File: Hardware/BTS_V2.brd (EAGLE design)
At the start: 113 x 79.4 mm, 57 parts, among them IC1 TPA3140D2PWP, IC2 BLK-MD-SPK-B, J1 SPKR_OUT, J2 RN52BoB_R, J3 RN52BoB_L, J6 HC-05, J7 PRT-10474, T3_2 TEENSY_3.1-3.2_DIL

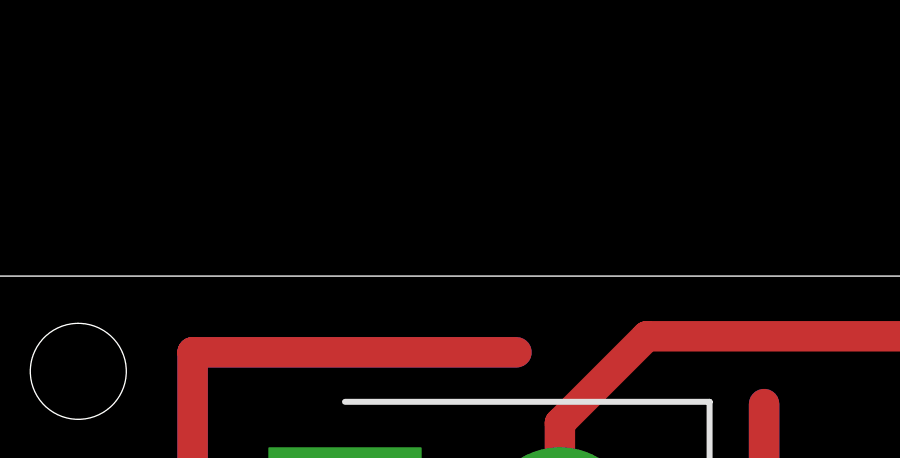
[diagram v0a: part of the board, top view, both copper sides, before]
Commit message: Created new XT-60 connector
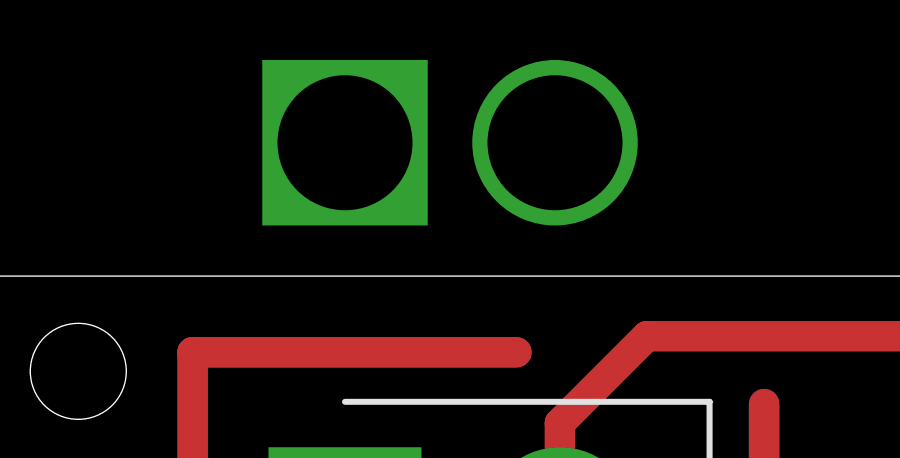
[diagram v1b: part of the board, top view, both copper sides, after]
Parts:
- added U$1: HK_XT-60, myLib:HOBBYKING_XT-60
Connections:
- net GND: now also U$1.P$1
- net VIN: now also U$1.P$2
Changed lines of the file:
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@@
 <element name="J4" library="SparkFun-Connectors" library_urn="urn:adsk.eagle:library:513" package="1X14" package3d_urn="urn:adsk.eagle:package:38183/1" value="" x="109.855" y="17.78" rot="R90"/>
 <element name="R16" library="resistor" library_urn="urn:adsk.eagle:library:348" package="R0603" package3d_urn="urn:adsk.eagle:package:26057/1" value="100R" x="100.33" y="45.72" rot="R180"/>
+<element name="U$1" library="myLib" package="HOBBYKING_XT-60" value="HK_XT-60" x="12.065" y="83.82"/>
 </elements>
 <signals>
@@
 <wire x1="33.79" y1="30.48" x2="38.735" y2="30.48" width="0.4064" layer="1"/>
 <contactref element="J4" pad="13"/>
+<contactref element="U$1" pad="P$1"/>
 <wire x1="99.695" y1="57.785" x2="109.855" y2="48.26" width="0" layer="19" extent="1-1"/>
 <wire x1="91.313" y1="52.07" x2="99.695" y2="57.785" width="0" layer="19" extent="1-1"/>
@@
 <wire x1="75.565" y1="26.924" x2="75.285" y2="26.3502125" width="0" layer="19" extent="1-1"/>
 <wire x1="71.755" y1="26.924" x2="72.035" y2="26.3502125" width="0" layer="19" extent="1-1"/>
+<wire x1="72.3646" y1="27.94" x2="71.29000625" y2="28.40499375" width="0" layer="19" extent="1-1"/>
 <wire x1="75.565" y1="28.956" x2="74.93" y2="27.94" width="0" layer="19" extent="1-1"/>
+<wire x1="70.1294" y1="27.94" x2="71.29000625" y2="28.40499375" width="0" layer="19" extent="1-1"/>
+<wire x1="76.9366" y1="27.94" x2="75.565" y2="26.924" width="0" layer="19" extent="1-1"/>
 <wire x1="75.145" y1="13.335" x2="75.285" y2="25.002" width="0" layer="19" extent="1-1"/>
 <wire x1="69.635" y1="13.335" x2="75.145" y2="13.335" width="0" layer="19" extent="1-1"/>
@@
 <wire x1="12.065" y1="71.12" x2="12.065" y2="52.705" width="0" layer="19" extent="1-1"/>
 <wire x1="12.7" y1="13.335" x2="33.64" y2="29.03" width="0" layer="19" extent="1-1"/>
+<wire x1="12.065" y1="83.82" x2="12.7" y2="13.335" width="0" layer="19" extent="1-1"/>
 </signal>
 <signal name="N$1">
@@
 <wire x1="19.228" y1="74.473" x2="22.1234" y2="77.3684" width="1.016" layer="1"/>
 <wire x1="22.1234" y1="77.3684" x2="55.245" y2="77.3684" width="1.016" layer="1"/>
+<contactref element="U$1" pad="P$2"/>
+<wire x1="19.065" y1="83.82" x2="19.228" y2="71.12" width="0" layer="19" extent="1-1"/>
 </signal>
 <signal name="PWRGOOD">

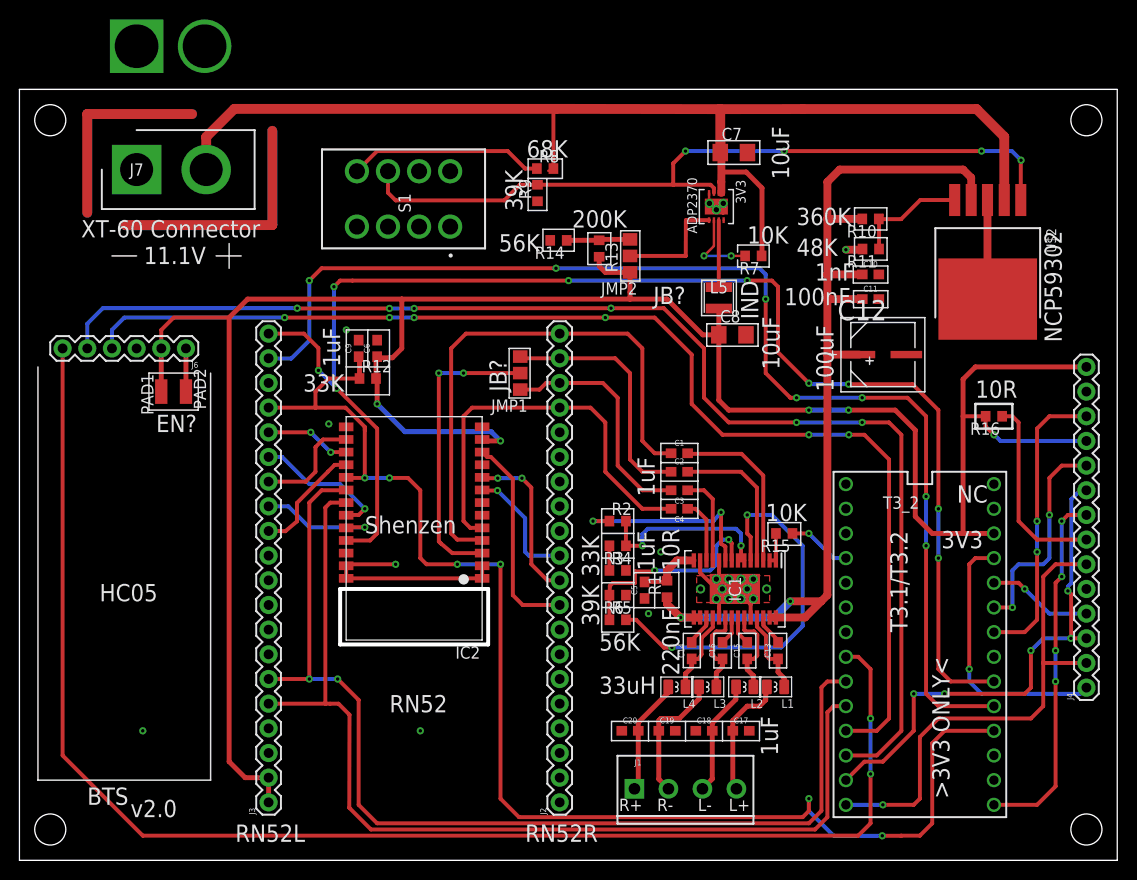
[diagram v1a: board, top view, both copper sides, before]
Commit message: added PA test code & modified V2 board files
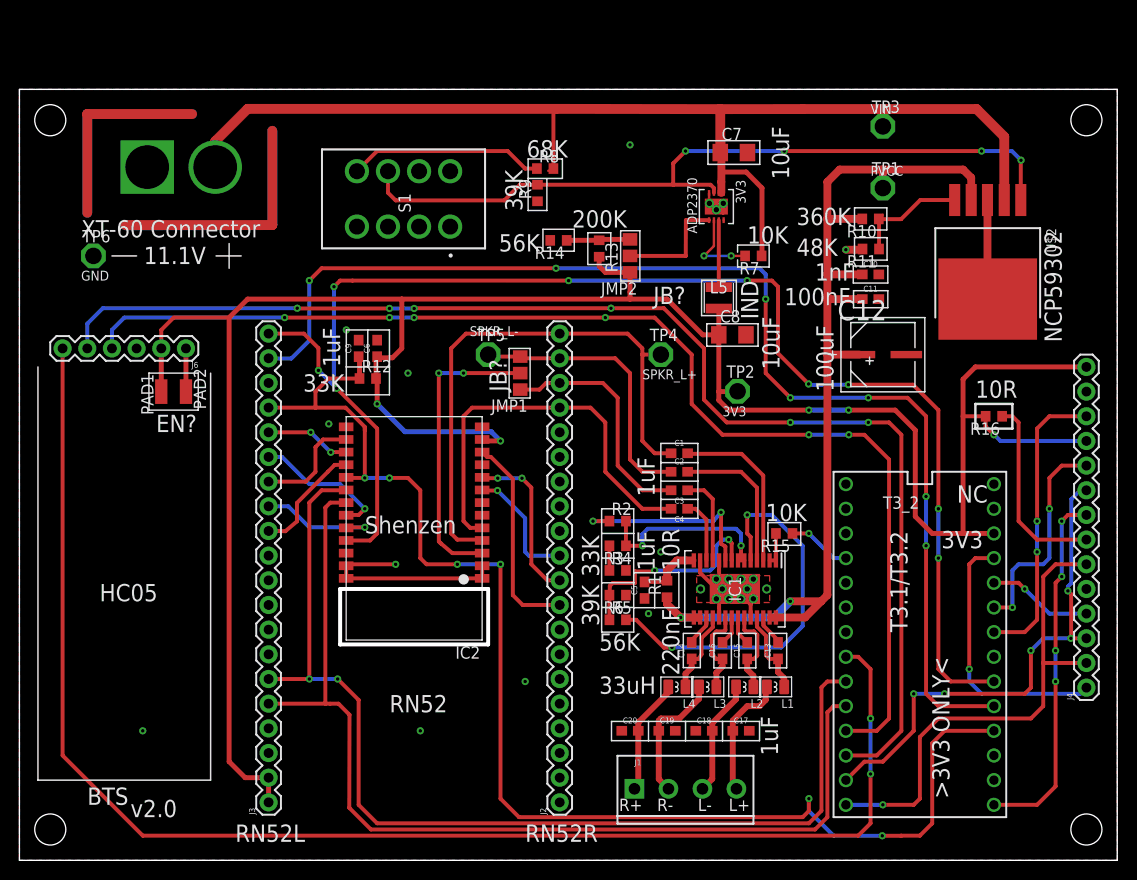
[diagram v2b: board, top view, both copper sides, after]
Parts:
- removed J7: PRT-10474, PRT-10474:SHDR2W320P716_1X2_1574X813X158
- added TP1, TP2, TP3, TP4, TP5, TP6: TPSPAD1-17, testpad:P1-17
- J4: value (none) -> TFT_CONNECTION
- moved U$1 12.5 mm to (13.2, 71.4)
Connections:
- net 3V3: now also TP2.TP
- net GND: now also TP6.TP; no longer J7.1
- net PVCC: now also TP1.TP
- net SPKR_L+: now also TP4.TP
- net SPKR_L-: now also TP5.TP
- net VIN: now also TP3.TP; no longer J7.2
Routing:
- net SPKR_L-: track 25.7 -> 29.0 mm
- net 3V3: track 248.3 -> 250.2 mm
- net PVCC: track 102.4 -> 104.3 mm
- net SPKR_L+: track 56.5 -> 58.4 mm
- net GND: vias 23 -> 26
- added copper zone on layer 16, net GND
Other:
- board text added: "GND"
- board text added: "PVCC"
- board text added: "SPKR_L+"
- board text added: "SPKR_L-"
- board text added: "VIN"

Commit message: Further error fixed
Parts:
- moved J6 12.7 mm to (4.45, 52.1), turned to 0 degrees
- moved PAD2 12.7 mm to (4.45, 48.3), turned to 0 degrees
- moved PAD1 7.62 mm to (6.99, 48.3), turned to 180 degrees
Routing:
- net HC_UART_RX: track 132.8 -> 157.4 mm
- net 3V3: track 250.2 -> 257.8 mm
- net HC_UART_TX: track 123.1 -> 121.2 mm
- net STATE: track 148.0 -> 149.3 mm
- net EN: track 4.45 -> 3.81 mm
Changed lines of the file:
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@@
 <wire x1="68.58" y1="14.3002" x2="68.58" y2="12.319" width="0.1524" layer="21"/>
 <wire x1="72.39" y1="14.3002" x2="72.39" y2="12.319" width="0.1524" layer="21"/>
-<text x="14.0716" y="44.0944" size="1.778" layer="21" font="vector">EN?</text>
+<text x="3.9116" y="43.4594" size="1.778" layer="21" font="vector">EN?</text>
 <wire x1="66.04" y1="42.926" x2="69.85" y2="42.926" width="0.1524" layer="21"/>
 <wire x1="69.85" y1="42.926" x2="69.85" y2="40.9448" width="0.1524" layer="21"/>
@@
 <wire x1="78.8162" y1="24.0284" x2="78.105" y2="24.0284" width="0.1524" layer="21"/>
 <wire x1="68.5038" y1="24.0284" x2="69.1896" y2="24.0284" width="0.1524" layer="21"/>
-<wire x1="13.335" y1="50.165" x2="18.415" y2="50.165" width="0.1524" layer="21"/>
-<wire x1="18.415" y1="50.165" x2="18.415" y2="46.355" width="0.1524" layer="21"/>
-<wire x1="18.415" y1="46.355" x2="13.335" y2="46.355" width="0.1524" layer="21"/>
-<wire x1="13.335" y1="46.355" x2="13.335" y2="50.165" width="0.1524" layer="21"/>
+<wire x1="8.255" y1="46.355" x2="3.175" y2="46.355" width="0.1524" layer="21"/>
+<wire x1="3.175" y1="46.355" x2="3.175" y2="50.165" width="0.1524" layer="21"/>
+<wire x1="3.175" y1="50.165" x2="8.255" y2="50.165" width="0.1524" layer="21"/>
+<wire x1="8.255" y1="50.165" x2="8.255" y2="46.355" width="0.1524" layer="21"/>
 <text x="22.225" y="1.905" size="1.778" layer="21" font="vector">RN52L</text>
 <text x="52.07" y="1.905" size="1.778" layer="21" font="vector">RN52R</text>
@@
 <attribute name="RESISTANCE" value="10K" x="55.499" y="63.8302" size="1.778" layer="27" rot="R180" display="off"/>
 </element>
-<element name="J6" library="SparkFun-Connectors" library_urn="urn:adsk.eagle:library:513" package="1X06" package3d_urn="urn:adsk.eagle:package:38009/1" value="HC-05" x="17.145" y="52.705" rot="R180">
-<attribute name="PROD_ID" value="CONN-08437" x="17.145" y="52.705" size="1.778" layer="27" rot="R180" display="off"/>
-</element>
-<element name="PAD1" library="wirepad" library_urn="urn:adsk.eagle:library:412" package="SMD1,27-2,54" package3d_urn="urn:adsk.eagle:package:30839/1" value="?" x="14.605" y="48.26"/>
-<element name="PAD2" library="wirepad" library_urn="urn:adsk.eagle:library:412" package="SMD1,27-2,54" package3d_urn="urn:adsk.eagle:package:30839/1" value="?" x="17.145" y="48.26" rot="R180"/>
+<element name="J6" library="SparkFun-Connectors" library_urn="urn:adsk.eagle:library:513" package="1X06" package3d_urn="urn:adsk.eagle:package:38009/1" value="HC-05" x="4.445" y="52.07">
+<attribute name="PROD_ID" value="CONN-08437" x="4.445" y="52.07" size="1.778" layer="27" display="off"/>
+</element>
+<element name="PAD1" library="wirepad" library_urn="urn:adsk.eagle:library:412" package="SMD1,27-2,54" package3d_urn="urn:adsk.eagle:package:30839/1" value="?" x="6.985" y="48.26" rot="R180"/>
+<element name="PAD2" library="wirepad" library_urn="urn:adsk.eagle:library:412" package="SMD1,27-2,54" package3d_urn="urn:adsk.eagle:package:30839/1" value="?" x="4.445" y="48.26"/>
 <element name="T3_2" library="Teensy_3_and_LC_Series_Boards_v1.4" package="TEENSY_3.0-3.2&amp;LC_DIL" value="TEENSY_3.1-3.2_DIL" x="92.71" y="22.225"/>
 <element name="R15" library="resistor" library_urn="urn:adsk.eagle:library:348" package="R0603" package3d_urn="urn:adsk.eagle:package:26057/1" value="10K" x="78.74" y="33.655" rot="R180">
@@
 <contactref element="J3" pad="1"/>
 <wire x1="39.37" y1="57.785" x2="23.495" y2="57.785" width="0.508" layer="1"/>
-<wire x1="14.605" y1="48.26" x2="14.605" y2="52.705" width="0.508" layer="1"/>
+<wire x1="6.985" y1="48.26" x2="6.985" y2="52.07" width="0.508" layer="1"/>
 <wire x1="23.495" y1="57.785" x2="21.59" y2="55.88" width="0.508" layer="1"/>
 <wire x1="21.59" y1="55.88" x2="21.59" y2="10.16" width="0.508" layer="1"/>
@@
 <via x="85.3694" y="46.355" extent="1-16" drill="0.35"/>
 <wire x1="85.3694" y1="46.355" x2="90.17" y2="46.355" width="0.508" layer="1"/>
-<wire x1="14.605" y1="52.705" x2="14.605" y2="54.61" width="0.4064" layer="1"/>
-<wire x1="14.605" y1="54.61" x2="15.875" y2="55.88" width="0.4064" layer="1"/>
-<wire x1="15.875" y1="55.88" x2="21.59" y2="55.88" width="0.4064" layer="1"/>
 <via x="81.28" y="46.355" extent="1-16" drill="0.35"/>
 <wire x1="62.865" y1="60.53" x2="62.865" y2="60.325" width="0.4064" layer="1"/>
@@
 <wire x1="73.9394" y1="48.2854" x2="73.914" y2="48.26" width="0.508" layer="1"/>
 <wire x1="73.914" y1="48.26" x2="72.006" y2="48.26" width="0.508" layer="1"/>
+<wire x1="8.255" y1="55.88" x2="6.985" y2="54.61" width="0.4064" layer="1"/>
+<wire x1="6.985" y1="54.61" x2="6.985" y2="52.07" width="0.4064" layer="1"/>
+<wire x1="21.59" y1="55.88" x2="8.255" y2="55.88" width="0.4064" layer="1"/>
 </signal>
 <signal name="N$65">
@@
 <wire x1="87.63" y1="8.89" x2="87.63" y2="14.605" width="0.4064" layer="16"/>
 <via x="87.63" y="14.605" extent="1-16" drill="0.35"/>
-<wire x1="4.445" y1="10.795" x2="4.445" y2="52.705" width="0.4064" layer="1"/>
+<wire x1="4.445" y1="10.795" x2="17.145" y2="52.07" width="0.4064" layer="1"/>
 <wire x1="87.63" y1="14.605" x2="87.63" y2="19.685" width="0.4064" layer="1"/>
 <wire x1="87.63" y1="19.685" x2="86.36" y2="20.955" width="0.4064" layer="1"/>
@@
 <contactref element="J6" pad="1"/>
 <contactref element="PAD2" pad="1"/>
-<wire x1="17.145" y1="48.26" x2="17.145" y2="52.705" width="0.508" layer="1"/>
+<wire x1="4.445" y1="48.26" x2="4.445" y2="52.07" width="0.508" layer="1"/>
 </signal>
 <signal name="HC_UART_TX">
@@
 <wire x1="89.535" y1="14.605" x2="88.265" y2="13.335" width="0.4064" layer="1"/>
 <wire x1="88.265" y1="13.335" x2="85.09" y2="13.335" width="0.4064" layer="1"/>
-<wire x1="9.525" y1="52.705" x2="9.525" y2="54.61" width="0.4064" layer="16"/>
-<wire x1="9.525" y1="54.61" x2="10.795" y2="55.88" width="0.4064" layer="16"/>
-<wire x1="10.795" y1="55.88" x2="27.305" y2="55.88" width="0.4064" layer="16"/>
+<wire x1="13.335" y1="55.88" x2="27.305" y2="55.88" width="0.4064" layer="16"/>
 <wire x1="85.3948" y1="43.815" x2="81.28" y2="43.815" width="0.4064" layer="16"/>
 <via x="81.28" y="43.815" extent="1-16" drill="0.35"/>
@@
 <wire x1="89.535" y1="41.275" x2="86.995" y2="43.815" width="0.4064" layer="1"/>
 <wire x1="86.995" y1="43.815" x2="85.3948" y2="43.815" width="0.4064" layer="1"/>
+<wire x1="12.065" y1="52.07" x2="12.065" y2="54.61" width="0.4064" layer="16"/>
+<wire x1="12.065" y1="54.61" x2="13.335" y2="55.88" width="0.4064" layer="16"/>
 </signal>
 <signal name="HC_UART_RX">
@@
 <wire x1="38.1" y1="56.8198" x2="28.6258" y2="56.8198" width="0.4064" layer="1"/>
 <wire x1="28.6258" y1="56.8198" x2="28.6004" y2="56.8452" width="0.4064" layer="1"/>
-<wire x1="6.985" y1="52.705" x2="6.985" y2="55.245" width="0.4064" layer="16"/>
-<wire x1="6.985" y1="55.245" x2="8.5852" y2="56.8452" width="0.4064" layer="16"/>
-<wire x1="8.5852" y1="56.8452" x2="28.6004" y2="56.8452" width="0.4064" layer="16"/>
+<wire x1="4.1402" y1="56.8452" x2="28.6004" y2="56.8452" width="0.4064" layer="16"/>
 <wire x1="88.265" y1="10.795" x2="90.805" y2="13.335" width="0.4064" layer="1"/>
 <via x="79.375" y="45.085" extent="1-16" drill="0.35"/>
@@
 <wire x1="90.805" y1="13.335" x2="90.805" y2="43.815" width="0.4064" layer="1"/>
 <wire x1="90.805" y1="43.815" x2="89.535" y2="45.085" width="0.4064" layer="1"/>
+<wire x1="4.1402" y1="56.8452" x2="2.54" y2="55.245" width="0.4064" layer="16"/>
+<wire x1="2.54" y1="55.245" x2="2.54" y2="48.895" width="0.4064" layer="16"/>
+<wire x1="2.54" y1="48.895" x2="3.81" y2="47.625" width="0.4064" layer="16"/>
+<wire x1="3.81" y1="47.625" x2="13.335" y2="47.625" width="0.4064" layer="16"/>
+<wire x1="13.335" y1="47.625" x2="14.605" y2="48.895" width="0.4064" layer="16"/>
+<wire x1="14.605" y1="48.895" x2="14.605" y2="52.07" width="0.4064" layer="16"/>
 </signal>
 <signal name="N$25">

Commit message: Error actually fixed
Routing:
- net STATE: track 149.3 -> 136.9 mm
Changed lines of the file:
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@@
 <contactref element="J6" pad="6"/>
 <contactref element="T3_2" pad="6"/>
-<wire x1="86.36" y1="2.54" x2="12.7" y2="2.54" width="0.4064" layer="1"/>
+<wire x1="21.59" y1="2.54" x2="86.36" y2="2.54" width="0.4064" layer="1"/>
 <wire x1="87.63" y1="8.89" x2="87.63" y2="3.81" width="0.4064" layer="1"/>
 <via x="87.63" y="8.89" extent="1-16" drill="0.35"/>
 <wire x1="87.63" y1="8.89" x2="87.63" y2="14.605" width="0.4064" layer="16"/>
 <via x="87.63" y="14.605" extent="1-16" drill="0.35"/>
-<wire x1="4.445" y1="10.795" x2="17.145" y2="52.07" width="0.4064" layer="1"/>
 <wire x1="87.63" y1="14.605" x2="87.63" y2="19.685" width="0.4064" layer="1"/>
 <wire x1="87.63" y1="19.685" x2="86.36" y2="20.955" width="0.4064" layer="1"/>
 <wire x1="86.36" y1="20.955" x2="85.09" y2="20.955" width="0.4064" layer="1"/>
-<wire x1="12.7" y1="2.54" x2="4.445" y2="10.795" width="0.4064" layer="1"/>
 <wire x1="86.36" y1="2.54" x2="87.63" y2="3.81" width="0.4064" layer="1"/>
+<wire x1="17.145" y1="52.07" x2="17.145" y2="6.985" width="0.4064" layer="1"/>
+<wire x1="17.145" y1="6.985" x2="21.59" y2="2.54" width="0.4064" layer="1"/>
 </signal>
 <signal name="EN">
